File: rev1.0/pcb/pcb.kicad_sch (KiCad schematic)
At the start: 15 parts, among them J1 AVR-ISP-6, SW1 SW_Push, U1 ATMEGA32U4, Y1 16MHz

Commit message: edited schematic and fixed constraints
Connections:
- net C13: no longer U1.8 (PB0)
- new net C14: U1.8 (PB0)
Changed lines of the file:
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@@
     )
   )
-  (global_label "C13" (shape input) (at 71.247 98.933 90) (fields_autoplaced)
-    (effects (font (size 1.27 1.27)) (justify left))
-    (property "Intersheet References" "${INTERSHEET_REFS}" (id 0) (at 71.1676 92.9262 90)
-      (effects (font (size 1.27 1.27)) (justify left) hide)
-    )
-  )
-  (global_label "C13" (shape output) (at 132.588 26.797 0) (fields_autoplaced)
+  (global_label "C14" (shape input) (at 71.247 98.933 90) (fields_autoplaced)
+    (effects (font (size 1.27 1.27)) (justify left))
+    (property "Intersheet References" "${INTERSHEET_REFS}" (id 0) (at 71.1676 92.8309 90)
+      (effects (font (size 1.27 1.27)) (justify left) hide)
+    )
+  )
+  (global_label "C14" (shape output) (at 132.588 26.797 0) (fields_autoplaced)
     (effects (font (size 1.27 1.27)) (justify left))
     (property "Intersheet References" "${INTERSHEET_REFS}" (id 0) (at 138.6901 26.7176 0)
@@
       (reference "D105") (unit 1) (value "BAV70") (footprint "Package_TO_SOT_SMD:SOT-23")
     )
-    (path "/c056f861-82ba-4a7e-9e72-5a4604669845/5439674f-83a9-4d9d-a767-d7965bd85a2f"
+    (path "/c056f861-82ba-4a7e-9e72-5a4604669845/f348a20a-82b1-4b09-af59-876b371d737b"
       (reference "D106") (unit 1) (value "BAV70") (footprint "Package_TO_SOT_SMD:SOT-23")
     )
-    (path "/c056f861-82ba-4a7e-9e72-5a4604669845/f348a20a-82b1-4b09-af59-876b371d737b"
+    (path "/c056f861-82ba-4a7e-9e72-5a4604669845/155a85ab-0052-4faa-b39d-826485ce9896"
       (reference "D107") (unit 1) (value "BAV70") (footprint "Package_TO_SOT_SMD:SOT-23")
     )
-    (path "/c056f861-82ba-4a7e-9e72-5a4604669845/155a85ab-0052-4faa-b39d-826485ce9896"
+    (path "/c056f861-82ba-4a7e-9e72-5a4604669845/e8ff04d5-920b-441f-8472-dbeb2358c0d7"
       (reference "D108") (unit 1) (value "BAV70") (footprint "Package_TO_SOT_SMD:SOT-23")
     )
-    (path "/c056f861-82ba-4a7e-9e72-5a4604669845/e8ff04d5-920b-441f-8472-dbeb2358c0d7"
+    (path "/c056f861-82ba-4a7e-9e72-5a4604669845/06ba327d-1471-4837-8194-dff19381ed4d"
       (reference "D109") (unit 1) (value "BAV70") (footprint "Package_TO_SOT_SMD:SOT-23")
     )
-    (path "/c056f861-82ba-4a7e-9e72-5a4604669845/06ba327d-1471-4837-8194-dff19381ed4d"
+    (path "/c056f861-82ba-4a7e-9e72-5a4604669845/f27ee04c-0530-4e51-a49b-bbc414265e15"
       (reference "D110") (unit 1) (value "BAV70") (footprint "Package_TO_SOT_SMD:SOT-23")
     )
-    (path "/c056f861-82ba-4a7e-9e72-5a4604669845/f27ee04c-0530-4e51-a49b-bbc414265e15"
+    (path "/c056f861-82ba-4a7e-9e72-5a4604669845/667d98ff-975e-4b44-87d4-965528898ffe"
       (reference "D111") (unit 1) (value "BAV70") (footprint "Package_TO_SOT_SMD:SOT-23")
     )
-    (path "/c056f861-82ba-4a7e-9e72-5a4604669845/667d98ff-975e-4b44-87d4-965528898ffe"
+    (path "/c056f861-82ba-4a7e-9e72-5a4604669845/eb396c18-f4cd-492d-ab4f-a0ada45298d5"
       (reference "D112") (unit 1) (value "BAV70") (footprint "Package_TO_SOT_SMD:SOT-23")
     )
-    (path "/c056f861-82ba-4a7e-9e72-5a4604669845/eb396c18-f4cd-492d-ab4f-a0ada45298d5"
+    (path "/c056f861-82ba-4a7e-9e72-5a4604669845/1a0eeafb-71b2-45f0-9e0d-009dc92a7cfe"
       (reference "D113") (unit 1) (value "BAV70") (footprint "Package_TO_SOT_SMD:SOT-23")
     )
-    (path "/c056f861-82ba-4a7e-9e72-5a4604669845/1a0eeafb-71b2-45f0-9e0d-009dc92a7cfe"
+    (path "/c056f861-82ba-4a7e-9e72-5a4604669845/2231c462-b6bb-43b1-a0d7-d4017e3f4feb"
       (reference "D114") (unit 1) (value "BAV70") (footprint "Package_TO_SOT_SMD:SOT-23")
     )
-    (path "/c056f861-82ba-4a7e-9e72-5a4604669845/2231c462-b6bb-43b1-a0d7-d4017e3f4feb"
+    (path "/c056f861-82ba-4a7e-9e72-5a4604669845/dd6a311b-d698-4f9a-9cda-b74981dd28b8"
       (reference "D115") (unit 1) (value "BAV70") (footprint "Package_TO_SOT_SMD:SOT-23")
     )
-    (path "/c056f861-82ba-4a7e-9e72-5a4604669845/dd6a311b-d698-4f9a-9cda-b74981dd28b8"
+    (path "/c056f861-82ba-4a7e-9e72-5a4604669845/43512e93-857c-42a1-9d3f-e16a44d77df2"
       (reference "D116") (unit 1) (value "BAV70") (footprint "Package_TO_SOT_SMD:SOT-23")
     )
-    (path "/c056f861-82ba-4a7e-9e72-5a4604669845/43512e93-857c-42a1-9d3f-e16a44d77df2"
+    (path "/c056f861-82ba-4a7e-9e72-5a4604669845/94c3c277-42e6-434c-84f3-116e945148bf"
       (reference "D117") (unit 1) (value "BAV70") (footprint "Package_TO_SOT_SMD:SOT-23")
     )
-    (path "/c056f861-82ba-4a7e-9e72-5a4604669845/94c3c277-42e6-434c-84f3-116e945148bf"
+    (path "/c056f861-82ba-4a7e-9e72-5a4604669845/4c67f2b5-10dc-4c73-aa28-c77bb571f6d2"
       (reference "D118") (unit 1) (value "BAV70") (footprint "Package_TO_SOT_SMD:SOT-23")
     )
-    (path "/c056f861-82ba-4a7e-9e72-5a4604669845/4c67f2b5-10dc-4c73-aa28-c77bb571f6d2"
+    (path "/c056f861-82ba-4a7e-9e72-5a4604669845/e17b61f2-97db-49a7-8fbc-9d7490ea5114"
       (reference "D119") (unit 1) (value "BAV70") (footprint "Package_TO_SOT_SMD:SOT-23")
     )
-    (path "/c056f861-82ba-4a7e-9e72-5a4604669845/e17b61f2-97db-49a7-8fbc-9d7490ea5114"
-      (reference "D120") (unit 1) (value "BAV70") (footprint "Package_TO_SOT_SMD:SOT-23")
-    )
     (path "/3ee7a193-1c79-43da-aa5f-923bdb6badb0/d11caa8e-0735-474f-86fc-57561ca10317"
-      (reference "D121") (unit 1) (value "SMF5.0CA") (footprint "Diode_SMD:D_SOD-123F")
+      (reference "D120") (unit 1) (value "SMF5.0CA") (footprint "Diode_SMD:D_SOD-123F")
     )
     (path "/3ee7a193-1c79-43da-aa5f-923bdb6badb0/85c9a0c5-f049-48b6-9560-e81ad0b53bcb"
@@
     )
     (path "/3ee7a193-1c79-43da-aa5f-923bdb6badb0/92fc67ca-dfa2-4746-9284-02d5c226cc5d"
-      (reference "J2") (unit 1) (value "USB4120-03-C") (footprint "0xcb:MOLEX_2130830005")
+      (reference "J2") (unit 1) (value "USB4120-03-C") (footprint "0xcb:GCT_USB4105_REVA")
     )
     (path "/c056f861-82ba-4a7e-9e72-5a4604669845/57b2c139-70ea-4a57-b03c-a17b8cbc199a"

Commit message: Did some columns and rows to controller
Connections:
- net C0: now also U1.18 (PD0); no longer U1.26 (PD6)
- net C1: now also U1.19 (PD1); no longer U1.27 (PD7)
- net C10: now also U1.30 (PB6); no longer U1.20 (PD2)
- net C11: now also U1.31 (PC6); no longer U1.19 (PD1)
- net C12: now also U1.32 (PC7); no longer U1.18 (PD0)
- net C2: now also U1.20 (PD2); no longer U1.28 (PB4)
- net C3: now also U1.21 (PD3); no longer U1.29 (PB5)
- net C4: now also U1.22 (PD5); no longer U1.30 (PB6)
- net C5: now also U1.25 (PD4); no longer U1.31 (PC6)
- net C6: now also U1.26 (PD6); no longer U1.32 (PC7)
- net C7: now also U1.27 (PD7); no longer U1.25 (PD4)
- net C8: now also U1.28 (PB4); no longer U1.22 (PD5)
- net C9: now also U1.29 (PB5); no longer U1.21 (PD3)
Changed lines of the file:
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@@
     )
   )
-  (global_label "C2" (shape output) (at 132.588 36.957 0) (fields_autoplaced)
+  (global_label "C8" (shape output) (at 132.588 36.957 0) (fields_autoplaced)
     (effects (font (size 1.27 1.27)) (justify left))
     (property "Intersheet References" "${INTERSHEET_REFS}" (id 0) (at 137.3853 36.8776 0)
@@
     )
   )
-  (global_label "C3" (shape output) (at 132.588 39.497 0) (fields_autoplaced)
+  (global_label "C9" (shape output) (at 132.588 39.497 0) (fields_autoplaced)
     (effects (font (size 1.27 1.27)) (justify left))
     (property "Intersheet References" "${INTERSHEET_REFS}" (id 0) (at 137.3853 39.4176 0)
@@
     )
   )
-  (global_label "C4" (shape output) (at 132.588 42.037 0) (fields_autoplaced)
+  (global_label "C10" (shape output) (at 132.588 42.037 0) (fields_autoplaced)
     (effects (font (size 1.27 1.27)) (justify left))
-    (property "Intersheet References" "${INTERSHEET_REFS}" (id 0) (at 137.3853 41.9576 0)
+    (property "Intersheet References" "${INTERSHEET_REFS}" (id 0) (at 138.5948 41.9576 0)
       (effects (font (size 1.27 1.27)) (justify left) hide)
     )
@@
     )
   )
-  (global_label "C5" (shape output) (at 132.588 48.387 0) (fields_autoplaced)
+  (global_label "C11" (shape output) (at 132.588 48.387 0) (fields_autoplaced)
     (effects (font (size 1.27 1.27)) (justify left))
-    (property "Intersheet References" "${INTERSHEET_REFS}" (id 0) (at 137.3853 48.3076 0)
+    (property "Intersheet References" "${INTERSHEET_REFS}" (id 0) (at 138.5948 48.3076 0)
       (effects (font (size 1.27 1.27)) (justify left) hide)
     )
   )
-  (global_label "C6" (shape output) (at 132.588 50.927 0) (fields_autoplaced)
+  (global_label "C12" (shape output) (at 132.588 50.927 0) (fields_autoplaced)
     (effects (font (size 1.27 1.27)) (justify left))
-    (property "Intersheet References" "${INTERSHEET_REFS}" (id 0) (at 137.3853 50.8476 0)
+    (property "Intersheet References" "${INTERSHEET_REFS}" (id 0) (at 138.5948 50.8476 0)
       (effects (font (size 1.27 1.27)) (justify left) hide)
     )
   )
-  (global_label "C12" (shape output) (at 132.588 54.737 0) (fields_autoplaced)
+  (global_label "C0" (shape output) (at 132.588 54.737 0) (fields_autoplaced)
     (effects (font (size 1.27 1.27)) (justify left))
-    (property "Intersheet References" "${INTERSHEET_REFS}" (id 0) (at 138.5948 54.6576 0)
+    (property "Intersheet References" "${INTERSHEET_REFS}" (id 0) (at 137.3853 54.6576 0)
       (effects (font (size 1.27 1.27)) (justify left) hide)
     )
   )
-  (global_label "C11" (shape output) (at 132.588 57.277 0) (fields_autoplaced)
+  (global_label "C1" (shape output) (at 132.588 57.277 0) (fields_autoplaced)
     (effects (font (size 1.27 1.27)) (justify left))
-    (property "Intersheet References" "${INTERSHEET_REFS}" (id 0) (at 138.5948 57.1976 0)
+    (property "Intersheet References" "${INTERSHEET_REFS}" (id 0) (at 137.3853 57.1976 0)
       (effects (font (size 1.27 1.27)) (justify left) hide)
     )
   )
-  (global_label "C10" (shape output) (at 132.588 59.817 0) (fields_autoplaced)
+  (global_label "C2" (shape output) (at 132.588 59.817 0) (fields_autoplaced)
     (effects (font (size 1.27 1.27)) (justify left))
-    (property "Intersheet References" "${INTERSHEET_REFS}" (id 0) (at 138.5948 59.7376 0)
+    (property "Intersheet References" "${INTERSHEET_REFS}" (id 0) (at 137.3853 59.7376 0)
       (effects (font (size 1.27 1.27)) (justify left) hide)
     )
   )
-  (global_label "C9" (shape output) (at 132.588 62.357 0) (fields_autoplaced)
+  (global_label "C3" (shape output) (at 132.588 62.357 0) (fields_autoplaced)
     (effects (font (size 1.27 1.27)) (justify left))
     (property "Intersheet References" "${INTERSHEET_REFS}" (id 0) (at 137.3853 62.2776 0)
@@
     )
   )
-  (global_label "C7" (shape output) (at 132.588 64.897 0) (fields_autoplaced)
+  (global_label "C5" (shape output) (at 132.588 64.897 0) (fields_autoplaced)
     (effects (font (size 1.27 1.27)) (justify left))
     (property "Intersheet References" "${INTERSHEET_REFS}" (id 0) (at 137.3853 64.8176 0)
@@
     )
   )
-  (global_label "C8" (shape output) (at 132.588 67.437 0) (fields_autoplaced)
+  (global_label "C4" (shape output) (at 132.588 67.437 0) (fields_autoplaced)
     (effects (font (size 1.27 1.27)) (justify left))
     (property "Intersheet References" "${INTERSHEET_REFS}" (id 0) (at 137.3853 67.3576 0)
@@
     )
   )
-  (global_label "C0" (shape output) (at 132.588 69.977 0) (fields_autoplaced)
+  (global_label "C6" (shape output) (at 132.588 69.977 0) (fields_autoplaced)
     (effects (font (size 1.27 1.27)) (justify left))
     (property "Intersheet References" "${INTERSHEET_REFS}" (id 0) (at 137.3853 69.8976 0)
@@
     )
   )
-  (global_label "C1" (shape output) (at 132.588 72.517 0) (fields_autoplaced)
+  (global_label "C7" (shape output) (at 132.588 72.517 0) (fields_autoplaced)
     (effects (font (size 1.27 1.27)) (justify left))
     (property "Intersheet References" "${INTERSHEET_REFS}" (id 0) (at 137.3853 72.4376 0)

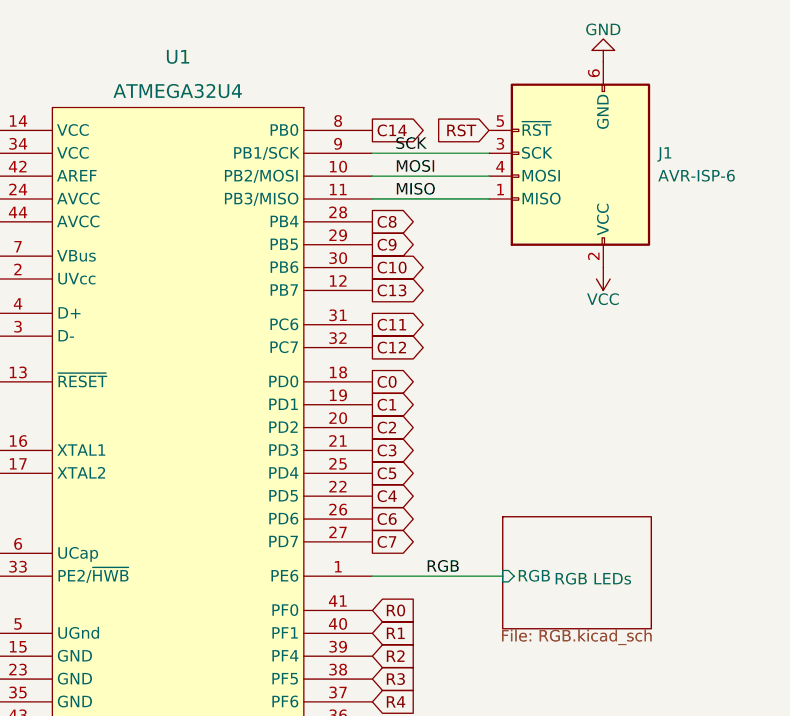
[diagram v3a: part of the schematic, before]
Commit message: Changed position of Controller
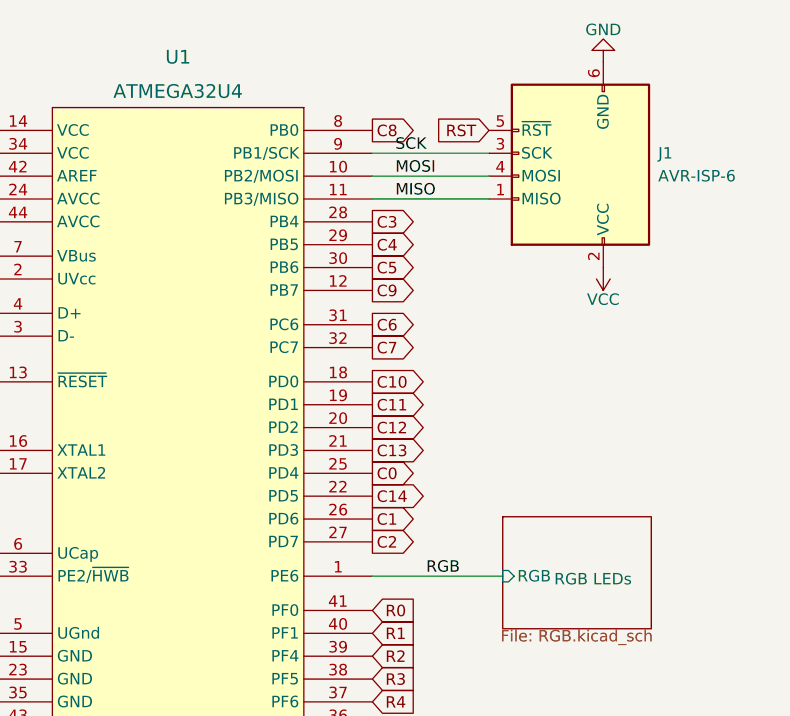
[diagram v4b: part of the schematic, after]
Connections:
- net C0: now also U1.25 (PD4); no longer U1.18 (PD0)
- net C1: now also U1.26 (PD6); no longer U1.19 (PD1)
- net C10: now also U1.18 (PD0); no longer U1.30 (PB6)
- net C11: now also U1.19 (PD1); no longer U1.31 (PC6)
- net C12: now also U1.20 (PD2); no longer U1.32 (PC7)
- net C13: now also U1.21 (PD3); no longer U1.12 (PB7)
- net C14: now also U1.22 (PD5); no longer U1.8 (PB0)
- net C2: now also U1.27 (PD7); no longer U1.20 (PD2)
- net C3: now also U1.28 (PB4); no longer U1.21 (PD3)
- net C4: now also U1.29 (PB5); no longer U1.22 (PD5)
- net C5: now also U1.30 (PB6); no longer U1.25 (PD4)
- net C6: now also U1.31 (PC6); no longer U1.26 (PD6)
- net C7: now also U1.32 (PC7); no longer U1.27 (PD7)
- net C8: now also U1.8 (PB0); no longer U1.28 (PB4)
- net C9: now also U1.12 (PB7); no longer U1.29 (PB5)
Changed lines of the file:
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@@
     )
   )
-  (global_label "C14" (shape output) (at 132.588 26.797 0) (fields_autoplaced)
+  (global_label "C8" (shape output) (at 132.588 26.797 0) (fields_autoplaced)
     (effects (font (size 1.27 1.27)) (justify left))
-    (property "Intersheet References" "${INTERSHEET_REFS}" (id 0) (at 138.6901 26.7176 0)
+    (property "Intersheet References" "${INTERSHEET_REFS}" (id 0) (at 137.3853 26.7176 0)
       (effects (font (size 1.27 1.27)) (justify left) hide)
     )
   )
-  (global_label "C8" (shape output) (at 132.588 36.957 0) (fields_autoplaced)
+  (global_label "C3" (shape output) (at 132.588 36.957 0) (fields_autoplaced)
     (effects (font (size 1.27 1.27)) (justify left))
     (property "Intersheet References" "${INTERSHEET_REFS}" (id 0) (at 137.3853 36.8776 0)
@@
     )
   )
-  (global_label "C9" (shape output) (at 132.588 39.497 0) (fields_autoplaced)
+  (global_label "C4" (shape output) (at 132.588 39.497 0) (fields_autoplaced)
     (effects (font (size 1.27 1.27)) (justify left))
     (property "Intersheet References" "${INTERSHEET_REFS}" (id 0) (at 137.3853 39.4176 0)
@@
     )
   )
-  (global_label "C10" (shape output) (at 132.588 42.037 0) (fields_autoplaced)
+  (global_label "C5" (shape output) (at 132.588 42.037 0) (fields_autoplaced)
     (effects (font (size 1.27 1.27)) (justify left))
-    (property "Intersheet References" "${INTERSHEET_REFS}" (id 0) (at 138.5948 41.9576 0)
+    (property "Intersheet References" "${INTERSHEET_REFS}" (id 0) (at 137.3853 41.9576 0)
       (effects (font (size 1.27 1.27)) (justify left) hide)
     )
   )
-  (global_label "C13" (shape output) (at 132.588 44.577 0) (fields_autoplaced)
+  (global_label "C9" (shape output) (at 132.588 44.577 0) (fields_autoplaced)
     (effects (font (size 1.27 1.27)) (justify left))
-    (property "Intersheet References" "${INTERSHEET_REFS}" (id 0) (at 138.5948 44.4976 0)
+    (property "Intersheet References" "${INTERSHEET_REFS}" (id 0) (at 137.3853 44.4976 0)
       (effects (font (size 1.27 1.27)) (justify left) hide)
     )
   )
-  (global_label "C11" (shape output) (at 132.588 48.387 0) (fields_autoplaced)
+  (global_label "C6" (shape output) (at 132.588 48.387 0) (fields_autoplaced)
     (effects (font (size 1.27 1.27)) (justify left))
-    (property "Intersheet References" "${INTERSHEET_REFS}" (id 0) (at 138.5948 48.3076 0)
+    (property "Intersheet References" "${INTERSHEET_REFS}" (id 0) (at 137.3853 48.3076 0)
       (effects (font (size 1.27 1.27)) (justify left) hide)
     )
   )
-  (global_label "C12" (shape output) (at 132.588 50.927 0) (fields_autoplaced)
+  (global_label "C7" (shape output) (at 132.588 50.927 0) (fields_autoplaced)
     (effects (font (size 1.27 1.27)) (justify left))
-    (property "Intersheet References" "${INTERSHEET_REFS}" (id 0) (at 138.5948 50.8476 0)
+    (property "Intersheet References" "${INTERSHEET_REFS}" (id 0) (at 137.3853 50.8476 0)
       (effects (font (size 1.27 1.27)) (justify left) hide)
     )
   )
-  (global_label "C0" (shape output) (at 132.588 54.737 0) (fields_autoplaced)
+  (global_label "C10" (shape output) (at 132.588 54.737 0) (fields_autoplaced)
     (effects (font (size 1.27 1.27)) (justify left))
-    (property "Intersheet References" "${INTERSHEET_REFS}" (id 0) (at 137.3853 54.6576 0)
+    (property "Intersheet References" "${INTERSHEET_REFS}" (id 0) (at 138.5948 54.6576 0)
       (effects (font (size 1.27 1.27)) (justify left) hide)
     )
   )
-  (global_label "C1" (shape output) (at 132.588 57.277 0) (fields_autoplaced)
+  (global_label "C11" (shape output) (at 132.588 57.277 0) (fields_autoplaced)
     (effects (font (size 1.27 1.27)) (justify left))
-    (property "Intersheet References" "${INTERSHEET_REFS}" (id 0) (at 137.3853 57.1976 0)
+    (property "Intersheet References" "${INTERSHEET_REFS}" (id 0) (at 138.5948 57.1976 0)
       (effects (font (size 1.27 1.27)) (justify left) hide)
     )
   )
-  (global_label "C2" (shape output) (at 132.588 59.817 0) (fields_autoplaced)
+  (global_label "C12" (shape output) (at 132.588 59.817 0) (fields_autoplaced)
     (effects (font (size 1.27 1.27)) (justify left))
-    (property "Intersheet References" "${INTERSHEET_REFS}" (id 0) (at 137.3853 59.7376 0)
+    (property "Intersheet References" "${INTERSHEET_REFS}" (id 0) (at 138.5948 59.7376 0)
       (effects (font (size 1.27 1.27)) (justify left) hide)
     )
   )
-  (global_label "C3" (shape output) (at 132.588 62.357 0) (fields_autoplaced)
+  (global_label "C13" (shape output) (at 132.588 62.357 0) (fields_autoplaced)
     (effects (font (size 1.27 1.27)) (justify left))
-    (property "Intersheet References" "${INTERSHEET_REFS}" (id 0) (at 137.3853 62.2776 0)
+    (property "Intersheet References" "${INTERSHEET_REFS}" (id 0) (at 138.5948 62.2776 0)
       (effects (font (size 1.27 1.27)) (justify left) hide)
     )
   )
-  (global_label "C5" (shape output) (at 132.588 64.897 0) (fields_autoplaced)
+  (global_label "C0" (shape output) (at 132.588 64.897 0) (fields_autoplaced)
     (effects (font (size 1.27 1.27)) (justify left))
     (property "Intersheet References" "${INTERSHEET_REFS}" (id 0) (at 137.3853 64.8176 0)
@@
     )
   )
-  (global_label "C4" (shape output) (at 132.588 67.437 0) (fields_autoplaced)
+  (global_label "C14" (shape output) (at 132.588 67.437 0) (fields_autoplaced)
     (effects (font (size 1.27 1.27)) (justify left))
-    (property "Intersheet References" "${INTERSHEET_REFS}" (id 0) (at 137.3853 67.3576 0)
+    (property "Intersheet References" "${INTERSHEET_REFS}" (id 0) (at 138.6901 67.3576 0)
       (effects (font (size 1.27 1.27)) (justify left) hide)
     )
   )
-  (global_label "C6" (shape output) (at 132.588 69.977 0) (fields_autoplaced)
+  (global_label "C1" (shape output) (at 132.588 69.977 0) (fields_autoplaced)
     (effects (font (size 1.27 1.27)) (justify left))
     (property "Intersheet References" "${INTERSHEET_REFS}" (id 0) (at 137.3853 69.8976 0)
@@
     )
   )
-  (global_label "C7" (shape output) (at 132.588 72.517 0) (fields_autoplaced)
+  (global_label "C2" (shape output) (at 132.588 72.517 0) (fields_autoplaced)
     (effects (font (size 1.27 1.27)) (justify left))
     (property "Intersheet References" "${INTERSHEET_REFS}" (id 0) (at 137.3853 72.4376 0)
